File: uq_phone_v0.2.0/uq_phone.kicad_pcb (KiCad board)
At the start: 6 copper layers, 118.2 x 108 mm, 193 parts, among them J2 124018312112A, J3 BM03B-ACHSS-GAN-TF_LF__SN_, J4 20279-001E-03, J5 20279-001E-03, J6 Conn_ARM_SWD_TagConnect_TC2030, J8 MCS-302S-C1, M1 C08-00A, Q1 MMBT3904LP-7, Q2 MMBT3904LP-7, SW1 SKTAAAE010, SW10 SKTAAAE010, SW11 SKTAAAE010, SW12 SKTAAAE010, SW13 SKTAAAE010, SW14 SKTAAAE010, SW15 SKTAAAE010, SW16 SKSCLCE010, SW17 SKTAAAE010, SW18 SKTAAAE010, SW19 SKTAAAE010, SW2 SKTAAAE010, SW20 SKTAAAE010, SW21 SKTAAAE010, SW22 SKSCLCE010, SW23 SKTAAAE010, SW24 SKTAAAE010, SW25 SKTAAAE010, SW26 SKTAAAE010, SW27 SKTAAAE010, SW28 SKTAAAE010, SW29 SKTAAAE010, SW3 SKTAAAE010, SW30 SKTAAAE010, SW31 SKTAAAE010, SW32 SKTAAAE010, SW33 SKTAAAE010, SW34 SKTAAAE010, SW35 SKTAAAE010, SW36 SKTAAAE010, SW37 SKTAAAE010, SW38 SKTAAAE010, SW39 SKTAAAE010, SW4 SKTAAAE010, SW40 SKTAAAE010, SW41 SKTAAAE010, SW5 SKTAAAE010, SW6 SKSCLCE010, SW7 SKTAAAE010, SW8 SKTAAAE010, SW9 SKTAAAE010, U1 TPS62162DSGR, U10 TPD8F003DQDR, U11 LSM6DSVTR, U12 DRV2603RUNR, U13 TS3A5018RSVR, U14 NAU88C22YG, U15 TPS22964CYZPR, U2 MCP73871-2CCI_ML, U3 BQ27441DRZR-G1A, U4 WP SNAP-IN BASE_6000636, U5 TXB0108YZPR2, U6 STM32H733VGHx, U7 TXB0108YZPR2, U8 TPD3F303DQDR, U9 MCP1664T-E/OT

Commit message: Minor Changes - new display
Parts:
- added OSC1: 19.2MHz, custom_footprints:OSC-SMD_4P-L2.0-W1.6-BL, F.Cu at (74.5, 30.1)
- added U16: BCR420UW6-7, BCR420UW6-7:SOT95P280X140-6N, F.Cu at (74.8, 49.5)
- C46: value 33pF -> 10nF
- moved LED10 68.4 mm to (60.4, 97.4)
- moved LED12 68.4 mm to (60.4, 92.8)
- moved LED16 68.4 mm to (63.0, 97.4)
- moved LED4 68.4 mm to (57.8, 97.4)
- moved LED6 68.4 mm to (57.8, 92.8)
- moved SW1 68.4 mm to (35.2, 104.0)
- moved SW10 68.4 mm to (40.0, 104.0)
- moved SW13 68.4 mm to (40.0, 94.7)
- moved SW15 68.4 mm to (40.0, 88.5)
- moved SW19 68.4 mm to (44.6, 104.0)
- moved SW23 68.4 mm to (44.6, 94.7)
- moved SW25 68.4 mm to (44.6, 88.5)
- moved SW28 68.4 mm to (49.4, 104.0)
- moved SW31 68.4 mm to (49.4, 94.7)
- moved SW33 68.4 mm to (49.4, 88.5)
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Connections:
- net DISP_LEDA renamed Net-(D2-K)
- net DISP_LEDK renamed Net-(U9-VFB)
- C27 pad 1: +3.3V_SW -> Net-(U9-VIN)
- C46 pad 1: MOB_SYS_CLK -> +1.8V
- J6 pad 6: unconnected-(J6-SWO-Pad6) -> SWO
- L2 pad 1: +3.3V_SW -> Net-(U9-VIN)
- R29 pad 1: GND -> unconnected-(R29-Pad1)
- U10 pad 12: unconnected-(U10-CH5_OUT-Pad12) -> uSD_SIM_CD
- U14 pad 11: MOB_SYS_CLK -> Net-(OSC1-OUT)
- U6 pad A7: PB_DPAD_UP -> SWO
- U6 pad B6: DISP_WR -> PB_DPAD_UP
- U6 pad C7: DISP_RES -> unconnected-(U6-PD3-PadC7)
- U6 pad D6: DISP_CS -> unconnected-(U6-PD7-PadD6)
- U6 pad D7: DISP_RD -> unconnected-(U6-PD4-PadD7)
- U6 pad D8: DISP_DB2 -> unconnected-(U6-PD0-PadD8)
- U6 pad E8: DISP_DB3 -> unconnected-(U6-PD1-PadE8)
- U6 pad G6: DISP_DB7 -> unconnected-(U6-PE10-PadG6)
- U6 pad G7: DISP_DB11 -> unconnected-(U6-PE14-PadG7)
- U6 pad G8: DISP_DB1 -> unconnected-(U6-PD15-PadG8)
- U6 pad G9: DISP_DC -> unconnected-(U6-PD11-PadG9)
- U6 pad H5: DISP_DB4 -> unconnected-(U6-PE7-PadH5)
- U6 pad H6: DISP_DB8 -> unconnected-(U6-PE11-PadH6)
- U6 pad H7: DISP_DB12 -> unconnected-(U6-PE15-PadH7)
- U6 pad H8: DISP_DB0 -> unconnected-(U6-PD14-PadH8)
- U6 pad H9: DISP_DB15 -> unconnected-(U6-PD10-PadH9)
- U6 pad J5: DISP_DB5 -> unconnected-(U6-PE8-PadJ5)
- U6 pad J6: DISP_DB9 -> unconnected-(U6-PE12-PadJ6)
- U6 pad J9: DISP_DB14 -> unconnected-(U6-PD9-PadJ9)
- U6 pad K5: DISP_DB6 -> unconnected-(U6-PE9-PadK5)
- U6 pad K6: DISP_DB10 -> unconnected-(U6-PE13-PadK6)
- U6 pad K9: DISP_DB13 -> unconnected-(U6-PD8-PadK9)
- U9 pad 4: DISP_BL -> unconnected-(U9-EN-Pad4)
- U9 pad 5: +3.3V_SW -> Net-(U9-VIN)

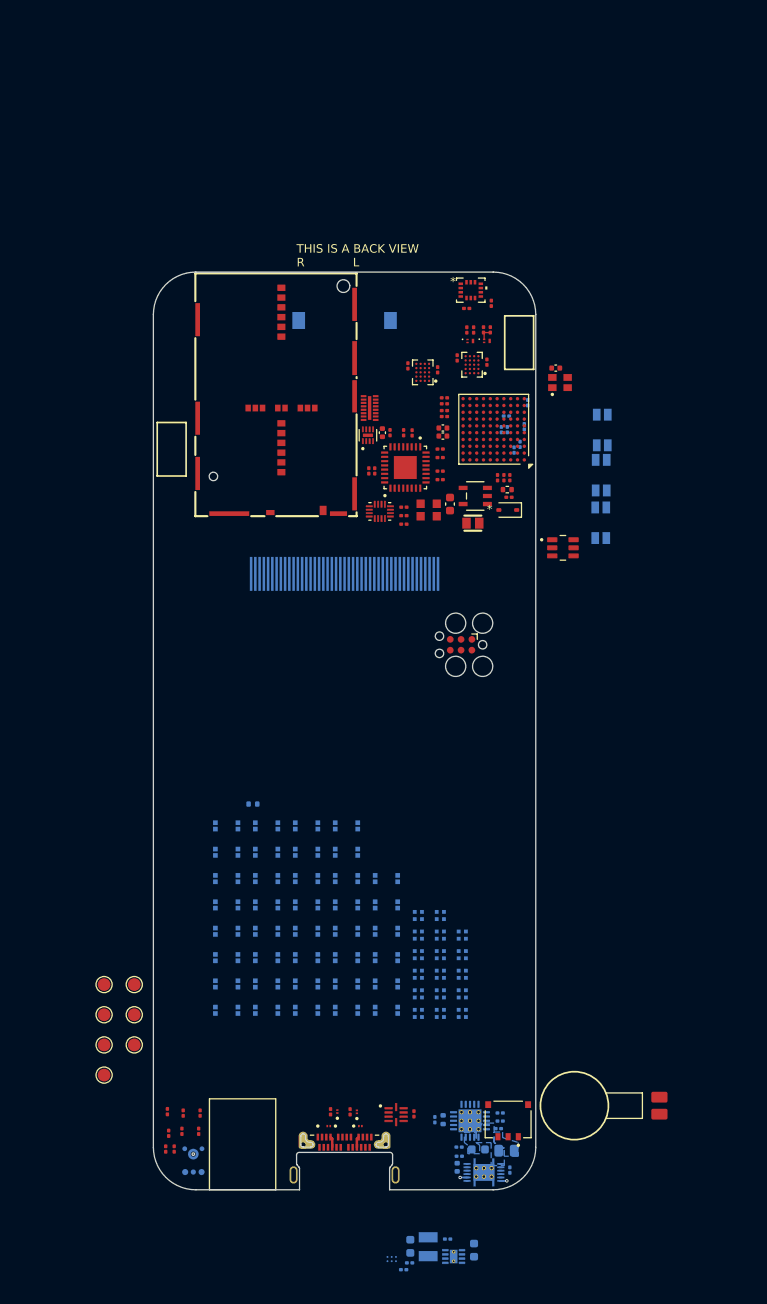
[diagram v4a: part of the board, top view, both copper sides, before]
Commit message: New HP jack, move stuff out for new arrangement
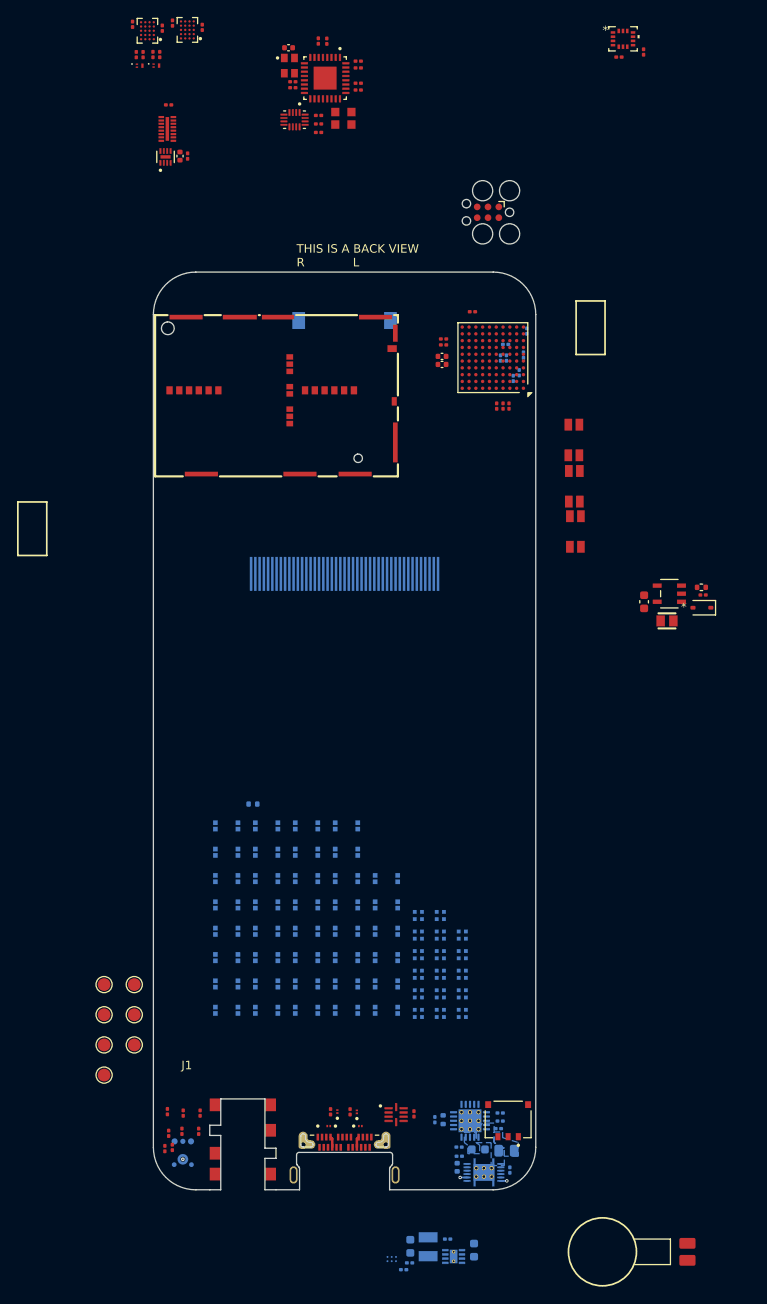
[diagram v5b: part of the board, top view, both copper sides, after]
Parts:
- removed U16: BCR420UW6-7, BCR420UW6-7:SOT95P280X140-6N
- added J1: PJ-242C, custom_footprints:PJ-242C, F.Cu at (37.2, 119.8)
- SW16, SW22, SW6: moved to F.Cu
- moved C22 51.7 mm to (32.4, -11.7)
- moved C23 51.7 mm to (28.9, -12.2)
- moved U7 51.7 mm to (30.6, -11.4)
- moved C21 51.6 mm to (24.2, -12.1)
- moved C24 51.6 mm to (27.7, -11.6)
- moved U5 51.6 mm to (25.9, -11.3)
- moved J6 51.0 mm to (66.0, 10.1)
- moved Q2 50.6 mm to (27.0, -7.20)
- moved R16 50.6 mm to (24.6, -8.49)
- moved R18 50.6 mm to (25.4, -8.49)
- moved Q1 50.6 mm to (25.0, -7.19)
- moved R17 50.6 mm to (26.6, -8.50)
- moved R19 50.6 mm to (27.4, -8.50)
- moved C46 49.1 mm to (42.6, -9.30), turned to 180 degrees
- moved OSC1 49.0 mm to (42.7, -7.20), turned to -90 degrees
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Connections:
- net Net-(D2-K) renamed DISP_LEDA
- net Net-(U9-VFB) renamed DISP_LEDK
- C27 pad 1: Net-(U9-VIN) -> +3.3V_SW
- L2 pad 1: Net-(U9-VIN) -> +3.3V_SW
- R29 pad 1: unconnected-(R29-Pad1) -> GND
- U9 pad 4: unconnected-(U9-EN-Pad4) -> DISP_BL
- U9 pad 5: Net-(U9-VIN) -> +3.3V_SW
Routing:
- net Net-(Q2-Pad1): track 1.64 -> 0.00 mm
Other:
- outline, holes or cut-outs redrawn

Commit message: New Layout
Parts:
- removed C27: 10uF, Capacitor_SMD:C_0603_1608Metric
- removed C28: 4.7uF, Capacitor_SMD:C_0201_0603Metric
- removed D2: PMEG2010EA, Diode_SMD:D_SOD-323
- removed Disp1: AFR240320A0-2.0INTM, custom_footprints:Display
- removed the J4 at (116.3, 24.4)
- removed the J5 at (138.6, 37.2)
- removed L2: 4.7uH, custom_footprints:IND-SMD_L2.0-W1.2_MTQH201208S4R7MBT
- removed R21: 4.7k, Resistor_SMD:R_0201_0603Metric
- removed R29: 3.83R, Resistor_SMD:R_0402_1005Metric
- removed U9: MCP1664T-E/OT, MCP1664T_E_OT:SOT-23-5_OT_MCH
- added C50: 100nF, Capacitor_SMD:C_0201_0603Metric, F.Cu at (56.4, 37.5)
- added C51: 100nF, Capacitor_SMD:C_0201_0603Metric, F.Cu at (56.5, 40.5)
- added DISP1: HS20HS072RX, custom_footprints:Display, B.Cu at (40.8, 53.9)
- added J10: 513382474, 513382474:CON_513382474, B.Cu at (138.5, 49.0)
- added J11: 513382474, 513382474:CON_513382474, B.Cu at (110.8, 53.0)
- added J7: 559092474, 559092474:CON_559092474, F.Cu at (25.7, 46.8)
- added J9: 559092474, 559092474:CON_559092474, F.Cu at (53.4, 42.8)
- added R4: 4.7k, Resistor_SMD:R_0201_0603Metric, F.Cu at (58.0, 32.8)
- added REF**: Art_large, custom_footprints:Art_large, F.Cu at (40.8, 84.3)
- added REF**: Art_small, custom_footprints:Art_small, F.Cu at (137.3, 40.5)
- added TP17: TestPoint, TestPoint:TestPoint_Pad_D1.5mm, F.Cu at (106.5, 39.8)
- added U16: TXB0108YZPR2, TXB0108YZPR2:YZP20, F.Cu at (53.9, 34.3)
- C1, C2, C3, C30, C31, C4, C5, C6, C7, L1, R1, R10, R11, R7, R8, R9, U1, U15, U2, U3: moved to F.Cu
- C25, C26, C29, C34, C35, C38, C39, C40, C41, C42, C43, C44, C45, C46, C47, FB1, FB2, OSC1, R32, R33, TP1, TP2, TP3, TP5, TP6, TP7, U11, U12, U13, U14: moved to B.Cu
- R5: footprint Resistor_SMD:R_0402_1005Metric -> Resistor_SMD:R_0201_0603Metric; moved to F.Cu
- U5: value TXB0108YZPR2 -> TCA9509MRVHR; footprint TXB0108YZPR2:YZP20 -> TCA9509MRVHR:RVH8_0P4X0P4
- moved C34 142.0 mm to (29.3, 122.1), turned to 0 degrees
- moved U11 140.2 mm to (30.3, 120.0), turned to 180 degrees
- moved C35 139.8 mm to (30.8, 122.1), turned to 180 degrees
- moved TP4 105.3 mm to (106.7, 50.6)
- moved C31 94.0 mm to (33.0, 43.4), turned to 90 degrees
- moved U1 93.5 mm to (30.4, 44.9), turned to -90 degrees
- moved C30 93.2 mm to (33.7, 43.4), turned to 90 degrees
- moved C1 92.8 mm to (35.0, 44.2)
- moved U15 90.6 mm to (33.4, 45.2), turned to 0 degrees
- moved R1 90.0 mm to (32.1, 45.8), turned to 90 degrees
- moved L1 88.2 mm to (31.6, 47.9), turned to 180 degrees
- moved C2 85.5 mm to (31.6, 50.0), turned to 0 degrees
- moved U3 82.0 mm to (42.7, 44.3)
- moved R8 81.7 mm to (45.8, 44.3), turned to 90 degrees
- moved C5 81.5 mm to (39.1, 44.3), turned to 180 degrees
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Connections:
- R22 pad 1: SDA -> SCL
- U4 pad 152: unconnected-(U4A-SAFE_PWR_REMOVE-Pad152) -> MOB_SAFE_PWR_REMOVE
- U4 pad 27: SIM_DATA -> SIM_CLK
- U4 pad 28: SIM_CLK -> SIM_DATA
- U7 pad A1: SCL -> unconnected-(U7-B2-PadA1)
- U7 pad A2: SDA -> unconnected-(U7-B1-PadA2)
- U7 pad A3: AUD_SDA -> unconnected-(U7-A1-PadA3)
- U7 pad A4: AUD_SCL -> unconnected-(U7-A2-PadA4)
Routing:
- net VUSB: track 2.57 -> 0.00 mm
- net SCL: track 0.83 -> 0.00 mm, vias 1 -> 0
- net FUEL_GPO: track 0.72 -> 0.00 mm, vias 1 -> 0
- removed copper zone on B.Cu, net Net-(U3-BAT)
- removed copper zone on B.Cu, net VBAT
- removed copper zone on B.Cu, net VUSB
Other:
- board size 118.2 x 108 mm -> 130.1 x 108 mm
- board text added: "SIM SOCKET"
- board text removed: "Socket Version"

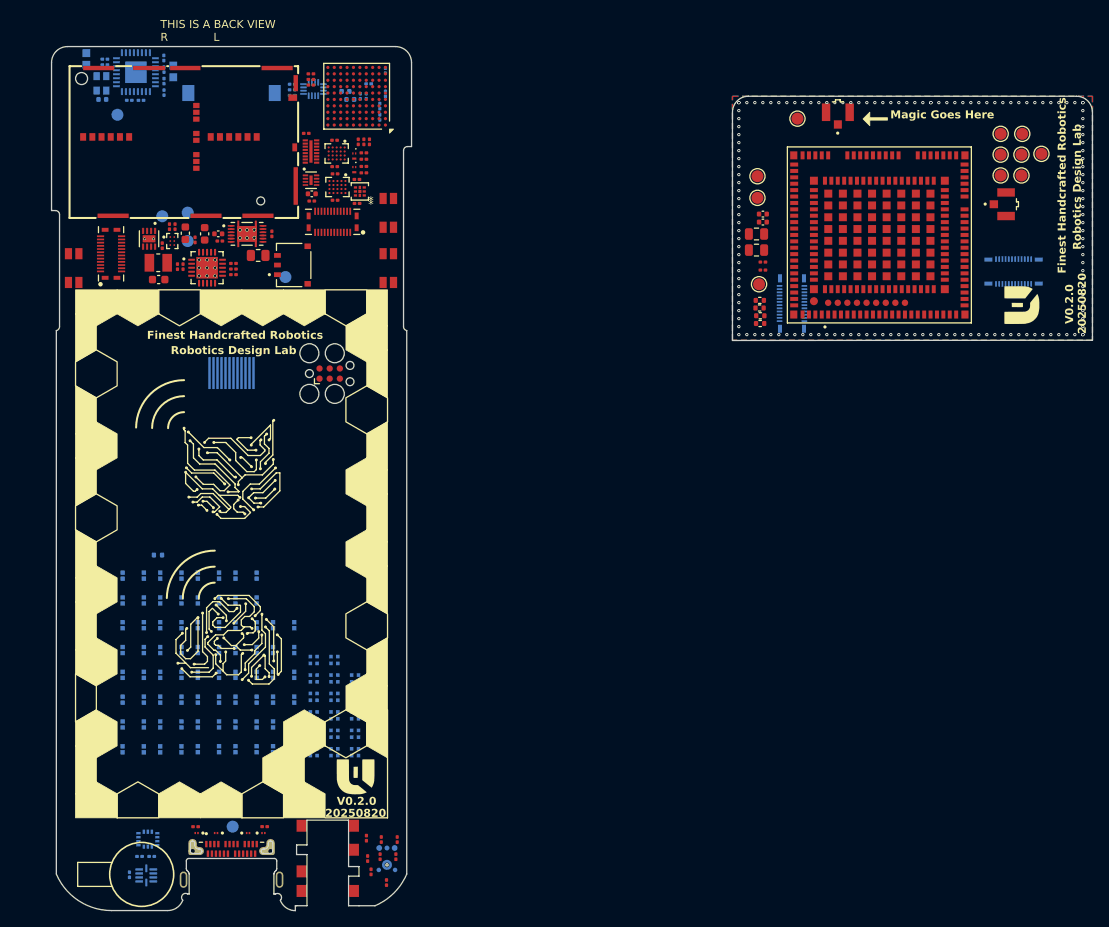
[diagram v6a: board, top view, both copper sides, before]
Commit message: Update layout and BL control
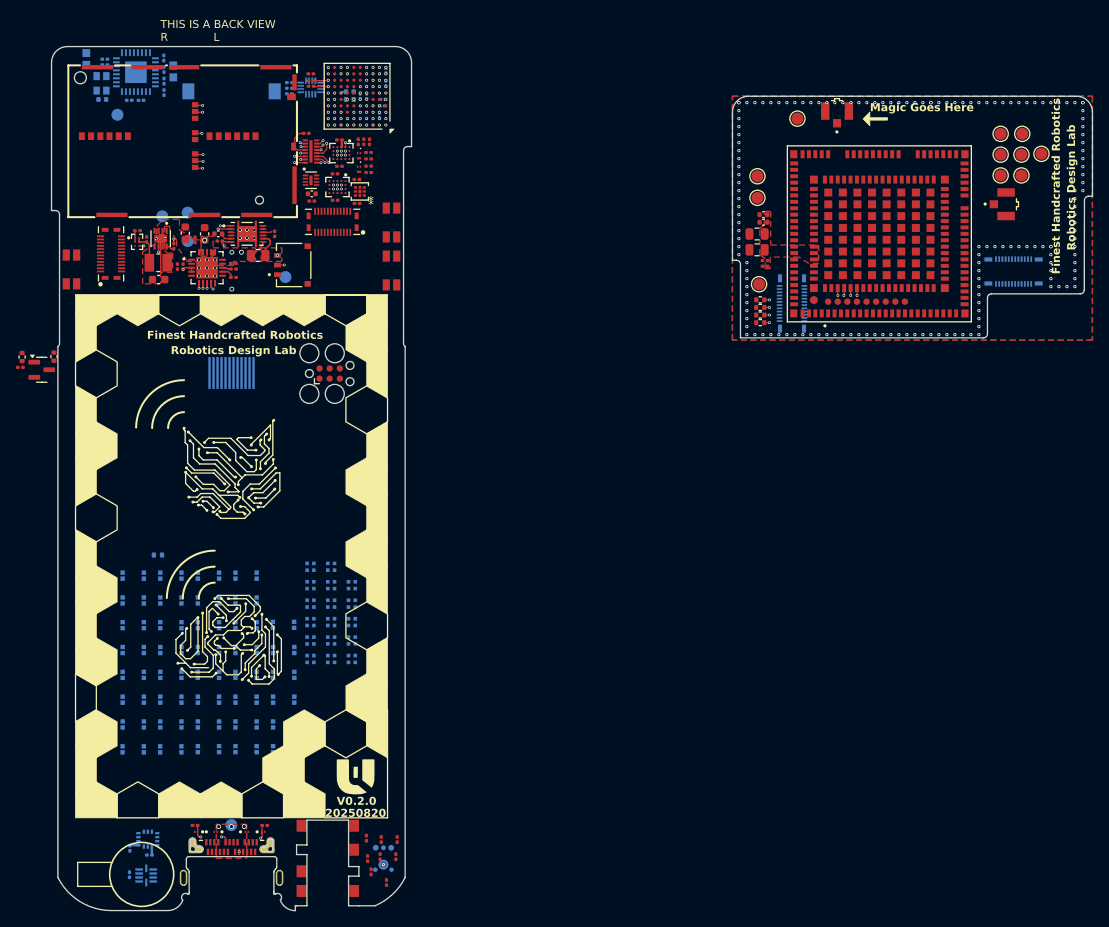
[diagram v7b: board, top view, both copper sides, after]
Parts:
- added Q3: S8050, Package_TO_SOT_SMD:SOT-23, F.Cu at (17.0, 61.3)
- added R21: 10k, Resistor_SMD:R_0201_0603Metric, F.Cu at (14.4, 61.0)
- added R26: 1k, Resistor_SMD:R_0402_1005Metric, F.Cu at (14.6, 59.7)
- added R27: 10R, Resistor_SMD:R_0402_1005Metric, F.Cu at (18.6, 59.7)
- moved LED10 11.7 mm to (53.2, 90.5)
- moved LED11 11.7 mm to (53.2, 88.2)
- moved LED12 11.7 mm to (53.2, 85.9)
- moved LED14 11.7 mm to (55.8, 95.1)
- moved LED16 11.7 mm to (55.8, 90.5)
- moved LED17 11.7 mm to (55.8, 88.2)
- moved LED2 11.7 mm to (50.6, 95.1)
- moved LED4 11.7 mm to (50.6, 90.5)
- moved LED5 11.7 mm to (50.6, 88.2)
- moved LED6 11.7 mm to (50.6, 85.9)
- moved LED8 11.7 mm to (53.2, 95.1)
- moved LED1 11.7 mm to (50.6, 97.4)
- moved LED13 11.7 mm to (55.8, 97.4)
- moved LED15 11.7 mm to (55.8, 92.8)
- moved LED3 11.7 mm to (50.6, 92.8)
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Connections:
- DISP1 pad 10: DISP_LEDA -> +3.3V_SW
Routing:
- net VUSB: track 0.00 -> 17.5 mm, vias 0 -> 7
- net VBAT: track 0.00 -> 16.6 mm, vias 0 -> 2
- net Net-(J8A-DAT1): track 0.00 -> 15.8 mm, vias 0 -> 2
- net Net-(J8A-DAT0): track 0.00 -> 15.4 mm, vias 0 -> 2
- net Net-(J8A-CLK): track 0.00 -> 14.6 mm, vias 0 -> 2
- net Net-(U4A-UART1_RX): track 0.00 -> 14.0 mm, vias 0 -> 2
- net Net-(J8A-DAT2): track 0.00 -> 14.0 mm, vias 0 -> 2
- net Net-(J8A-CMD): track 0.00 -> 13.8 mm, vias 0 -> 2
- net Net-(J8A-CD/DAT3): track 0.00 -> 13.7 mm, vias 0 -> 2
- net Net-(U4A-UART1_TX): track 0.00 -> 12.8 mm, vias 0 -> 2
- net Net-(U3-BAT): track 0.00 -> 12.1 mm, vias 0 -> 2
- net Net-(U4A-UART1_CTS): track 0.00 -> 11.6 mm, vias 0 -> 2
- net +3.3V: track 0.00 -> 10.8 mm, vias 0 -> 8
- net uSD_DAT0: track 0.00 -> 10.4 mm, vias 0 -> 2
- net Net-(U4A-UART1_RTS): track 0.00 -> 10.4 mm, vias 0 -> 2
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- added copper zone on F.Cu, net +3.3V
- added copper zone on F.Cu, net MCP_OUT
- added copper zone on F.Cu, net Net-(U1-SW)
- added copper zone on F.Cu, net Net-(U3-BAT)
- added copper zone on F.Cu, net VBAT
- added copper zone on F.Cu, net VUSB
- added copper zone on In1.Cu, net VUSB
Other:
- outline, holes or cut-outs redrawn

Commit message: Several Hours of Routing
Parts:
- added ?: , , F.Cu at (85.9, 39.5)
- added ?: , , F.Cu at (85.9, 23.8)
- added REF**: MountingHole, custom_footprints:Mounting, F.Cu at (19.1, 24.5)
- added REF**: MountingHole, custom_footprints:Mounting, F.Cu at (19.1, 40.1)
- C23, C24, U7: moved to B.Cu
- R27: value 10R -> 5R
- moved R23 30.2 mm to (34.4, 50.5), turned to -90 degrees
- moved R24 30.0 mm to (33.6, 50.5), turned to -90 degrees
- moved J10 19.6 mm to (120.2, 42.2)
- moved C10 19.6 mm to (89.1, 41.5)
- moved C11 19.6 mm to (89.1, 40.8)
- moved C12 19.6 mm to (88.1, 39.5)
- moved C13 19.6 mm to (88.1, 37.5)
- moved C8 19.6 mm to (88.9, 36.0)
- moved C9 19.6 mm to (88.9, 35.0)
- moved J11 19.6 mm to (92.5, 46.2)
- moved J4 19.6 mm to (98.1, 22.1)
- moved R12 19.6 mm to (88.5, 47.6)
- moved R13 19.6 mm to (88.5, 45.7)
- moved R14 19.6 mm to (88.5, 48.5)
- moved R15 19.6 mm to (88.5, 46.6)
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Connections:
- J11 pad 1: VBAT -> GND
- J11 pad 10: +1.8V -> GND
- J11 pad 11: +1.8V -> GND
- J11 pad 12: +1.8V -> GND
- J11 pad 13: GND -> VBAT
- J11 pad 14: GND -> VBAT
- J11 pad 15: GND -> VBAT
- J11 pad 16: GND -> VBAT
- J11 pad 17: GND -> VBAT
- J11 pad 18: GND -> VBAT
- J11 pad 19: GND -> VBAT
- J11 pad 2: VBAT -> GND
- J11 pad 20: GND -> +1.8V
- J11 pad 21: GND -> +1.8V
- J11 pad 22: GND -> +1.8V
- J11 pad 23: GND -> +1.8V
- J11 pad 3: VBAT -> GND
- J11 pad 4: VBAT -> GND
- J11 pad 5: VBAT -> GND
- J11 pad 6: VBAT -> GND
- J11 pad 7: VBAT -> GND
- J11 pad 8: VBAT -> GND
- J11 pad 9: +1.8V -> GND
- J7 pad 1: VBAT -> GND
- J7 pad 10: +1.8V -> GND
- J7 pad 11: +1.8V -> GND
- J7 pad 12: +1.8V -> GND
- J7 pad 13: GND -> VBAT
- J7 pad 14: GND -> VBAT
- J7 pad 15: GND -> VBAT
- J7 pad 16: GND -> VBAT
- J7 pad 17: GND -> VBAT
- J7 pad 18: GND -> VBAT
- J7 pad 19: GND -> VBAT
- J7 pad 2: VBAT -> GND
- J7 pad 20: GND -> +1.8V
- J7 pad 21: GND -> +1.8V
- J7 pad 22: GND -> +1.8V
- J7 pad 23: GND -> +1.8V
- J7 pad 3: VBAT -> GND
- J7 pad 4: VBAT -> GND
- J7 pad 5: VBAT -> GND
- J7 pad 6: VBAT -> GND
- J7 pad 7: VBAT -> GND
- J7 pad 8: VBAT -> GND
- J7 pad 9: +1.8V -> GND
- J9 pad 21: unconnected-(J9-Pad21) -> SIM_RST
- J9 pad 22: unconnected-(J9-Pad22) -> SIM_CLK
- J9 pad 23: unconnected-(J9-Pad23) -> SIM_DATA
- J9 pad 24: unconnected-(J9-Pad24) -> SIM_VDD
- U16 pad A1: MCU_DCD -> MCU_DTR
- U16 pad A2: MCU_DSR -> MCU_DCD
- U16 pad A3: MOB_DSR -> MOB_DCD
- U16 pad A4: MOB_DCD -> MOB_DTR
- U16 pad B1: MCU_RXD -> MCU_DSR
- U16 pad B2: MCU_DTR -> MCU_TXD
- U16 pad B3: MOB_DTR -> MOB_TXD
- U16 pad B4: MOB_RXD -> MOB_DSR
- U16 pad C2: MCU_TXD -> MCU_RTS
- U16 pad C3: MOB_TXD -> MOB_RTS
- U16 pad D2: MCU_RTS -> MCU_CTS
- U16 pad D3: MOB_RTS -> MOB_CTS
- U16 pad E1: MCU_CTS -> MCU_RXD
- U16 pad E4: MOB_CTS -> MOB_RXD
- U6 pad C7: unconnected-(U6-PD3-PadC7) -> MCU_DCD
- U6 pad D8: unconnected-(U6-PD0-PadD8) -> MCU_DTR
- U6 pad G10: MCP_STAT1 -> MCP_PG
- U6 pad G9: unconnected-(U6-PD11-PadG9) -> FUEL_GPO
- U6 pad H10: MCP_STAT2 -> MCP_STAT1
- U6 pad H9: unconnected-(U6-PD10-PadH9) -> MCP_STAT2
- U6 pad J10: MCU_DTR -> unconnected-(U6-PD13-PadJ10)
- U6 pad J8: MCP_PG -> unconnected-(U6-PB13-PadJ8)
- U6 pad K10: MCU_DCD -> unconnected-(U6-PD12-PadK10)
- U6 pad K8: FUEL_GPO -> unconnected-(U6-PB12-PadK8)
- U7 pad B1: HP_DET_MCU -> MCU_AUD_OUT_L_H
- U7 pad B2: MOB_WAKE_H -> MCU_AUD_BCLK_H
- U7 pad B3: MOB_WAKE_L -> MCU_AUD_BCLK_L
- U7 pad B4: HP_DET -> MCU_AUD_OUT_L
- U7 pad D2: MCU_AUD_BCLK_H -> MOB_WAKE_H
- U7 pad D3: MCU_AUD_BCLK_L -> MOB_WAKE_L
- U7 pad E2: MCU_AUD_OUT_L_H -> HP_DET_MCU
- U7 pad E3: MCU_AUD_OUT_L -> HP_DET
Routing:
- net FUEL_GPO: track 0.00 -> 43.7 mm, vias 1 -> 2
- net MCP_STAT1: track 2.48 -> 46.1 mm, vias 2 -> 3
- net MCP_STAT2: track 2.48 -> 44.9 mm, vias 2 -> 3
- net MCP_PG: track 0.63 -> 42.2 mm
- net AUD_OUT: track 0.00 -> 29.8 mm, vias 0 -> 2
- net AUD_IN: track 0.00 -> 28.5 mm, vias 0 -> 2
- net AUD_BCLK: track 0.00 -> 28.3 mm, vias 0 -> 2
- net HP_DET: track 0.00 -> 26.8 mm, vias 0 -> 2
- net AUD_SYNC: track 0.00 -> 25.9 mm, vias 0 -> 2
- net SIM_VDD: track 0.00 -> 20.1 mm, vias 0 -> 2
- net Net-(J8B-SIM_1_RST): track 0.00 -> 12.5 mm, vias 0 -> 2
- net MCU_AUD_BCLK_H: track 0.00 -> 11.6 mm
- net MCU_AUD_SYNC_H: track 0.00 -> 11.4 mm
- net BAT_THERM: track 0.85 -> 11.9 mm, vias 1 -> 2
- net Net-(J8B-SIM_1_DATA): track 0.00 -> 10.6 mm, vias 0 -> 2
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- added copper zone on F.Cu, net +1.8V
- added copper zone on In2.Cu, net VBAT
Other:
- board size 130.1 x 108 mm -> 111.8 x 108.6 mm
